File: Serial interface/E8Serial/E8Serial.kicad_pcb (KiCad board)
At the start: 2 copper layers, 125 x 113 mm, 52 parts, among them J1 Conn_01x04_Male, J2 Conn_01x04_Male, J3 Conn_01x04_Male, J4 Conn_01x04_Male, Q1 BC548, Q2 BC548, Q3 BC548, SW1 NDB2, SW2 NDB1, SW3 PARITY ODD_EVEN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

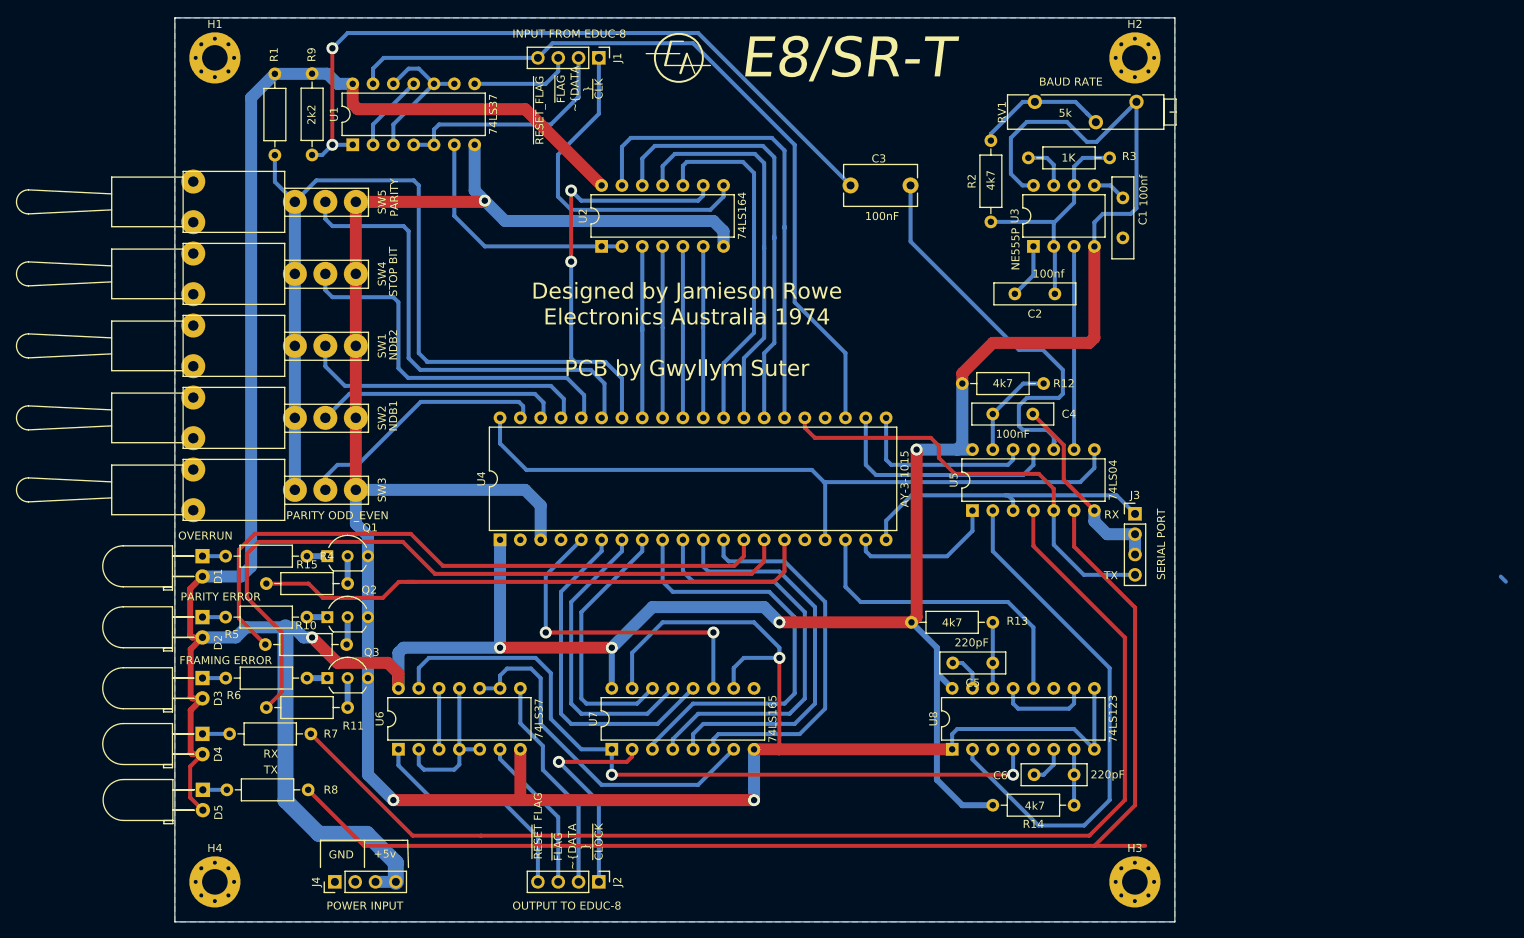
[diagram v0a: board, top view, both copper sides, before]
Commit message: Schematic update 2024-04-14 plus fixes
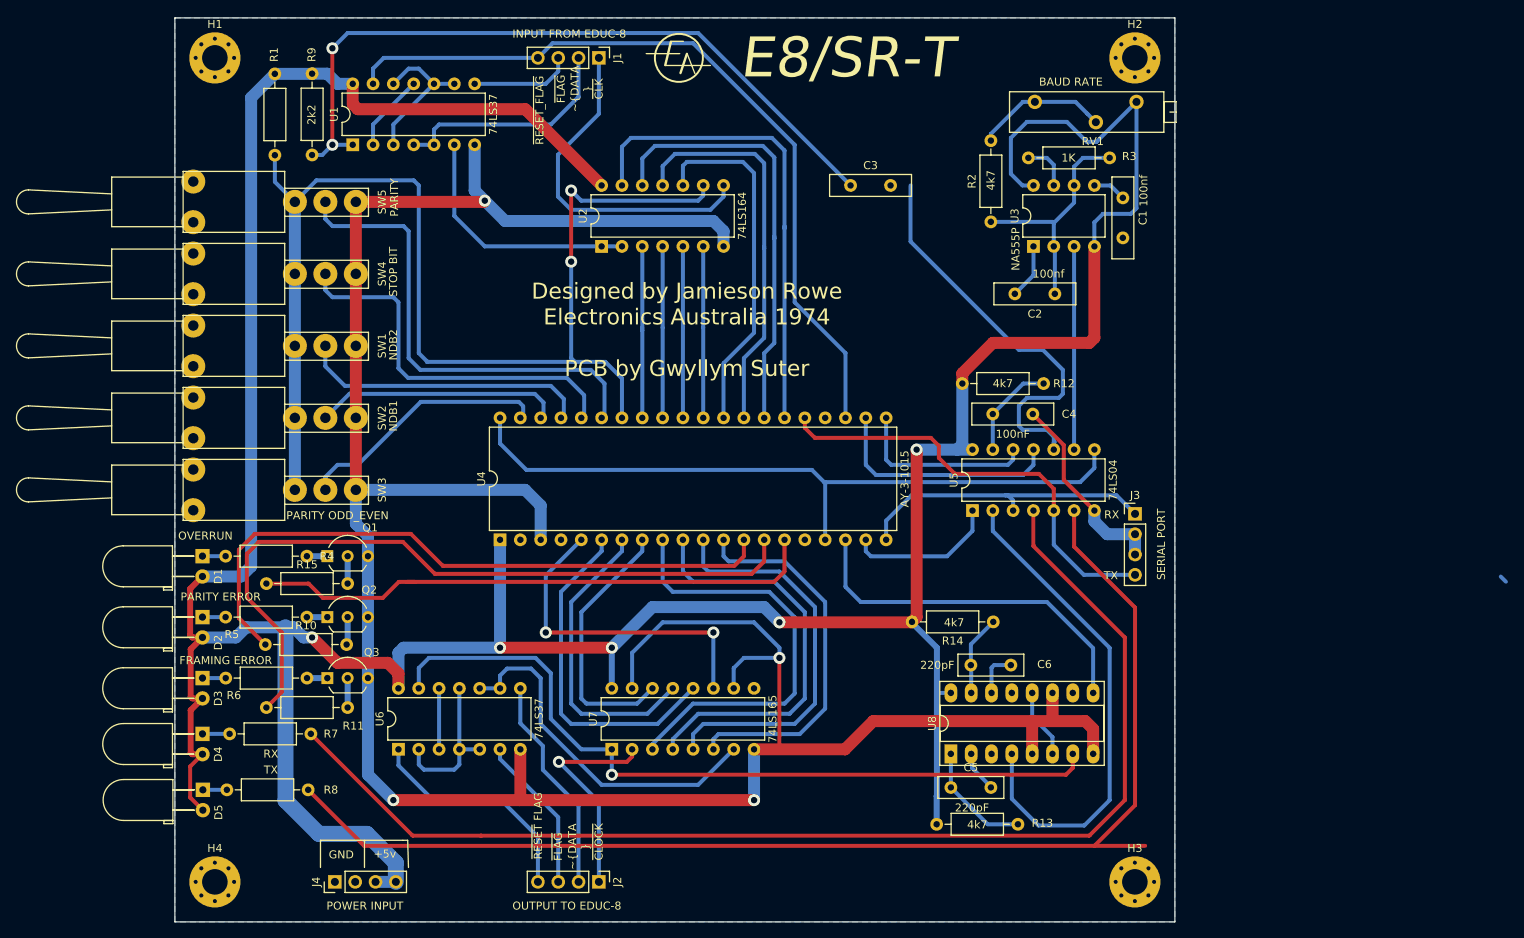
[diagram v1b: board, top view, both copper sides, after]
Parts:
- C3: footprint Capacitor_THT:C_Disc_D9.0mm_W5.0mm_P7.50mm -> Capacitor_THT:C_Disc_D10.0mm_W2.5mm_P5.00mm
- RV1: footprint Potentiometer_THT:Potentiometer_Bourns_3005_Horizontal -> Potentiometer_THT:Potentiometer_Bourns_3006P_Horizontal
- U3: value NE555P -> NA555P
- U8: value 74LS123 -> DM9602; footprint Package_DIP:DIP-16_W7.62mm -> Package_DIP:DIP-16_W7.62mm_Socket_LongPads
- moved R13 25.4 mm to (145.4, 147.8)
- moved R14 25.0 mm to (142.3, 122.5)
- moved C6 18.8 mm to (139.5, 127.9), turned to 0 degrees
- moved C5 16.4 mm to (137.0, 143.2), turned to 0 degrees
- moved U8 0.59 mm to (137.0, 139.0)
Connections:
- net ~CLR renamed ~{CLR}
- net ~INPUT_CLOCK renamed ~{INPUT_CLOCK}
- net ~INPUT_DATA renamed ~{INPUT_DATA}
- net ~INPUT_FLAG renamed ~{INPUT_FLAG}
- net ~INPUT_RESET_FLAG renamed ~{INPUT_RESET_FLAG}
- net ~OUTPUT_FLAG renamed ~{OUTPUT_FLAG}
- net ~OUTPUT_RESET_FLAG renamed ~{OUTPUT_RESET_FLAG}
- net ~OUT_CLOCK renamed ~{OUT_CLOCK}
- U4 pad 16: Net-(U4-Pad16) -> unconnected-(U4-Pad16)
- U4 pad 18: ~RDA -> ~{RDA}
- U4 pad 2: Net-(U4-Pad2) -> unconnected-(U4-Pad2)
- U4 pad 24: Net-(U4-Pad24) -> unconnected-(U4-Pad24)
- U4 pad 4: Net-(U4-Pad4) -> unconnected-(U4-Pad4)
- U7 pad 9: Net-(U7-Pad9) -> unconnected-(U7-Pad9)
- U8 pad 1: GND -> Net-(C5-Pad1)
- U8 pad 10: Net-(U8-Pad10) -> unconnected-(U8-Pad10)
- U8 pad 11: Net-(U8-Pad11) -> GND
- U8 pad 12: ~RDA -> Net-(U8-Pad12)
- U8 pad 13: Net-(U8-Pad10) -> unconnected-(U8-Pad13)
- U8 pad 14: Net-(C5-Pad1) -> Net-(C6-Pad2)
- U8 pad 15: Net-(C5-Pad2) -> Net-(C6-Pad1)
- U8 pad 2: Net-(U5-Pad2) -> Net-(C5-Pad2)
- U8 pad 3: Net-(U8-Pad3) -> unconnected-(U8-Pad3)
- U8 pad 4: SL -> Net-(U5-Pad2)
- U8 pad 5: Net-(U8-Pad5) -> GND
- U8 pad 6: Net-(C6-Pad2) -> Net-(U8-Pad12)
- U8 pad 7: Net-(C6-Pad1) -> SL
- U8 pad 9: GND -> ~{RDA}
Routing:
- net ~{RDA}: track 0.00 -> 45.6 mm
- net ~RDA: track 39.1 -> 0.00 mm
- net Net-(U8-Pad10): track 12.0 -> 0.00 mm
- net Net-(U8-Pad12): track 0.00 -> 8.67 mm
- net SL: track 91.8 -> 98.2 mm, vias 2 -> 1
- net Net-(C5-Pad1): track 8.25 -> 14.5 mm
- net +5V: track 467.4 -> 463.8 mm
- net Net-(C6-Pad1): track 6.98 -> 10.1 mm
- net Net-(U5-Pad2): track 65.4 -> 62.8 mm
- net GND: track 352.2 -> 353.8 mm
- net Net-(C6-Pad2): track 4.89 -> 5.71 mm
- net Net-(C5-Pad2): track 4.89 -> 5.68 mm
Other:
- net class Default removed
- board text added: "~{CLK}"
- board text added: "~{CLOCK}"
- board text added: "~{DATA }"
- board text added: "~{FLAG}"
- board text added: "~{RESET_FLAG}"
- board text added: "~{RESET} FLAG"
- board text removed: "~CLK"
- board text removed: "~CLOCK"
- board text removed: "~DATA"
- board text removed: "~FLAG"
- board text removed: "~RESET FLAG"
- board text removed: "~RESET_FLAG"
